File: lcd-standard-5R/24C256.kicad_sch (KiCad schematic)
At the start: 10 parts, among them U6 CAT24C256

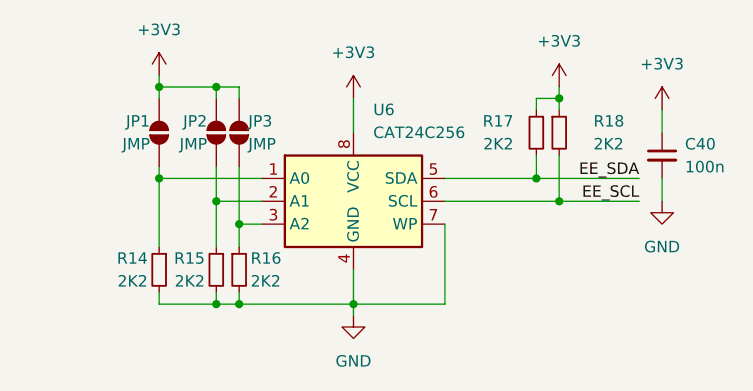
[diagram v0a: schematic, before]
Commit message: Change MCU to STM32H743
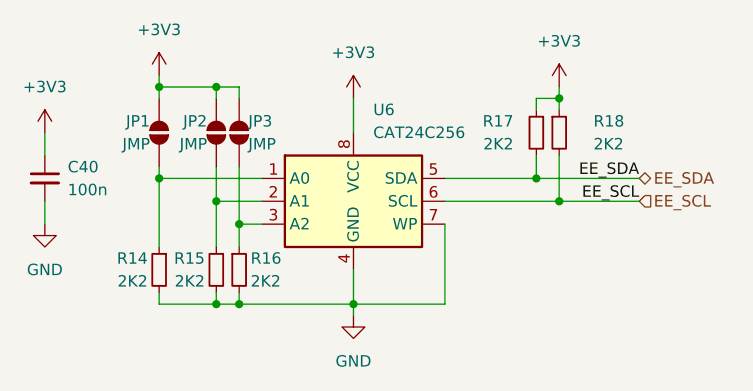
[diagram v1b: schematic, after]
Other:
- moved on the sheet: C40
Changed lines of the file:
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@@
 	(wire
 		(pts
-			(xy 172.72 90.17) (xy 172.72 92.71)
+			(xy 104.14 92.71) (xy 104.14 95.25)
 		)
 		(stroke
@@
 	(wire
 		(pts
-			(xy 172.72 100.33) (xy 172.72 97.79)
+			(xy 104.14 102.87) (xy 104.14 100.33)
 		)
 		(stroke
@@
 		)
 	)
+	(hierarchical_label "EE_SDA"
+		(shape bidirectional)
+		(at 170.18 97.79 0)
+		(fields_autoplaced yes)
+		(effects
+			(font
+				(size 1.27 1.27)
+			)
+			(justify left)
+		)
+	)
+	(hierarchical_label "EE_SCL"
+		(shape input)
+		(at 170.18 100.33 0)
+		(fields_autoplaced yes)
+		(effects
+			(font
+				(size 1.27 1.27)
+			)
+			(justify left)
+		)
+	)
 	(symbol
 		(lib_id "Jumper:SolderJumper_2_Open")
@@
 	(symbol
 		(lib_id "power:+3V3")
-		(at 172.72 90.17 0)
+		(at 104.14 92.71 0)
 		(unit 1)
 		(exclude_from_sim no)
@@
 		(fields_autoplaced yes)
 		(property "Reference" "#PWR072"
-			(at 172.72 93.98 0)
+			(at 104.14 96.52 0)
 			(effects
 				(font
@@
 		)
 		(property "Value" "+3V3"
-			(at 172.72 85.09 0)
+			(at 104.14 87.63 0)
 			(effects
 				(font
@@
 		)
 		(property "Footprint" ""
-			(at 172.72 90.17 0)
+			(at 104.14 92.71 0)
 			(effects
 				(font
@@
 		)
 		(property "Datasheet" ""
-			(at 172.72 90.17 0)
+			(at 104.14 92.71 0)
 			(effects
 				(font
@@
 		)
 		(property "Description" "Power symbol creates a global label with name \"+3V3\""
-			(at 172.72 90.17 0)
+			(at 104.14 92.71 0)
 			(effects
 				(font
@@
 	(symbol
 		(lib_id "Device:C_Small")
-		(at 172.72 95.25 0)
+		(at 104.14 97.79 0)
 		(unit 1)
 		(exclude_from_sim no)
@@
 		(fields_autoplaced yes)
 		(property "Reference" "C40"
-			(at 175.26 93.9862 0)
+			(at 106.68 96.5262 0)
 			(effects
 				(font
@@
 		)
 		(property "Value" "100n"
-			(at 175.26 96.5262 0)
+			(at 106.68 99.0662 0)
 			(effects
 				(font
@@
 		)
 		(property "Footprint" "Capacitor_SMD:C_0402_1005Metric"
-			(at 172.72 95.25 0)
+			(at 104.14 97.79 0)
 			(effects
 				(font
@@
 		)
 		(property "Datasheet" "~"
-			(at 172.72 95.25 0)
+			(at 104.14 97.79 0)
 			(effects
 				(font
@@
 		)
 		(property "Description" "Unpolarized capacitor, small symbol"
-			(at 172.72 95.25 0)
+			(at 104.14 97.79 0)
 			(effects
 				(font
@@
 		)
 		(property "JLCPCB Part #" "C1525"
-			(at 172.72 95.25 0)
+			(at 104.14 97.79 0)
 			(effects
 				(font
@@
 	(symbol
 		(lib_id "power:GND")
-		(at 172.72 100.33 0)
+		(at 104.14 102.87 0)
 		(unit 1)
 		(exclude_from_sim no)
@@
 		(fields_autoplaced yes)
 		(property "Reference" "#PWR073"
-			(at 172.72 106.68 0)
+			(at 104.14 109.22 0)
 			(effects
 				(font
@@
 		)
 		(property "Value" "GND"
-			(at 172.72 105.41 0)
+			(at 104.14 107.95 0)
 			(effects
 				(font
@@
 		)
 		(property "Footprint" ""
-			(at 172.72 100.33 0)
+			(at 104.14 102.87 0)
 			(effects
 				(font
@@
 		)
 		(property "Datasheet" ""
-			(at 172.72 100.33 0)
+			(at 104.14 102.87 0)
 			(effects
 				(font
@@
 		)
 		(property "Description" "Power symbol creates a global label with name \"GND\" , ground"
-			(at 172.72 100.33 0)
-			(effects
-				(font
+			(at 104.14 102.87 0)
+			(effects
+				(font

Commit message: Change 10P CTP to omron type
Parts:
- C40: JLCPCB Part # C1525 -> C307331
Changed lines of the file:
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@@
 			)
 		)
-		(property "JLCPCB Part #" "C1525"
+		(property "JLCPCB Part #" "C307331"
 			(at 104.14 97.79 0)
 			(effects

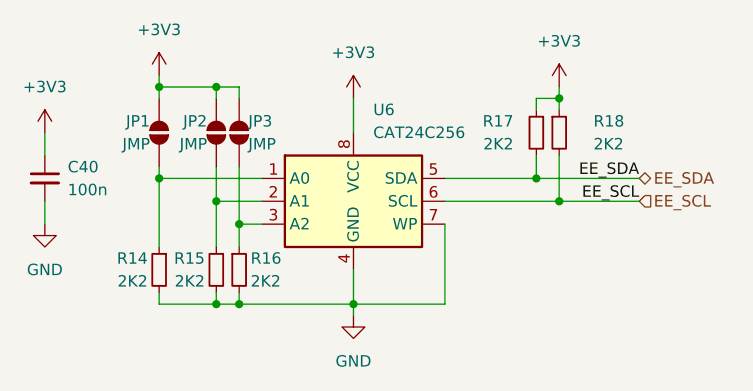
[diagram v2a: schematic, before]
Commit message: Finished SDRAM, LCD (need checkup with CubeIDE), RTP touch controll
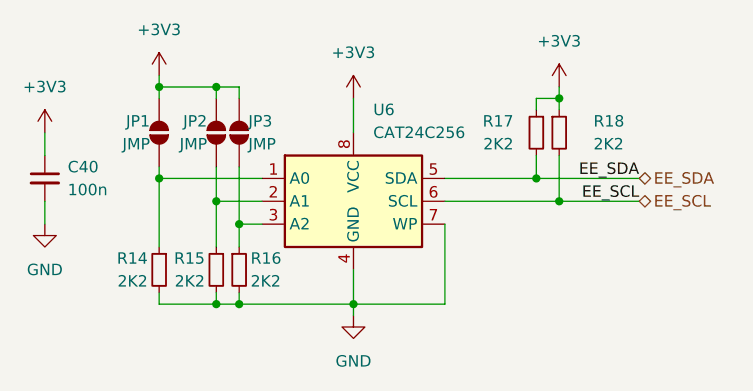
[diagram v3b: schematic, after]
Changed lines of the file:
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@@
 	)
 	(hierarchical_label "EE_SCL"
-		(shape input)
+		(shape bidirectional)
 		(at 170.18 100.33 0)
 		(fields_autoplaced yes)

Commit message: Add QSPI Flash trace length matching to 5 inch LCD
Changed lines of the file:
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@@
 (kicad_sch
-	(version 20231120)
+	(version 20250114)
 	(generator "eeschema")
-	(generator_version "8.0")
+	(generator_version "9.0")
 	(paper "A4")
 	(junction
@@
 	(label "EE_SDA"
 		(at 170.18 97.79 180)
-		(fields_autoplaced yes)
 		(effects
 			(font
@@
 	(label "EE_SCL"
 		(at 170.18 100.33 180)
-		(fields_autoplaced yes)
 		(effects
 			(font
@@
 		(shape bidirectional)
 		(at 170.18 97.79 0)
-		(fields_autoplaced yes)
 		(effects
 			(font
@@
 		(shape bidirectional)
 		(at 170.18 100.33 0)
-		(fields_autoplaced yes)
 		(effects
 			(font

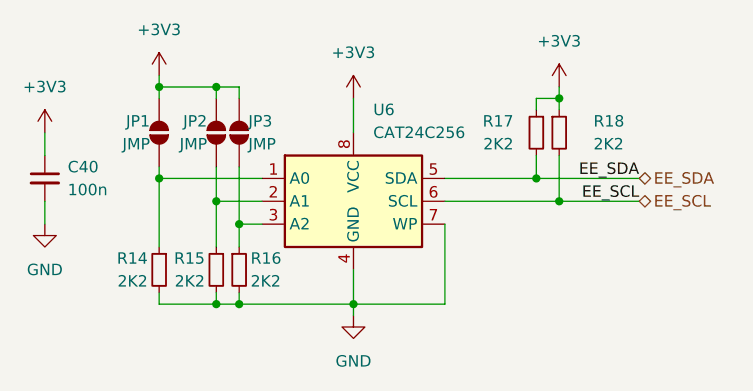
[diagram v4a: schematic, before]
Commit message: relocate SDRAM
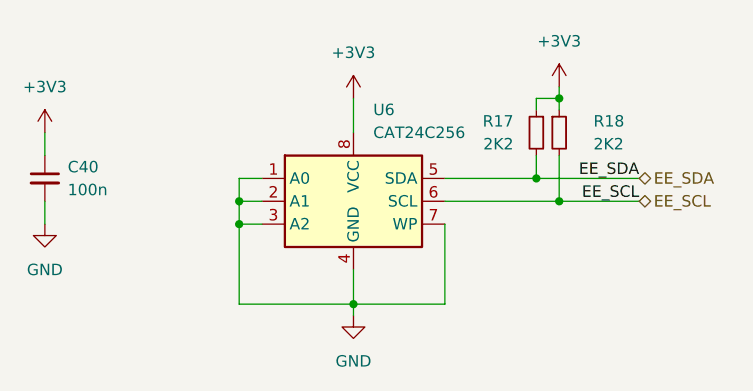
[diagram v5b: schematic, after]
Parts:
- removed JP1, JP2, JP3: JMP, Jumper:SolderJumper-2_P1.3mm_Open_RoundedPad1.0x1.5mm, symbol Jumper:SolderJumper_2_Open
- removed R14, R15, R16: 2K2, Resistor_SMD:R_0402_1005Metric, symbol Device:R_Small
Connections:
- net GND: now also U6.1 (A0), U6.2 (A1), U6.3 (A2)
